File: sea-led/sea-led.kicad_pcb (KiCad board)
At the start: 2 copper layers, 0 parts

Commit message: Lots of footprint updates
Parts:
- added C1: 0.1uF, Capacitor_SMD:C_0805_2012Metric, F.Cu at (118.3, 56.6)
- added C10: 100uF, Capacitor_SMD:C_1206_3216Metric, F.Cu at (91.1, 74.0)
- added C11: 4.7uF, Capacitor_SMD:C_0805_2012Metric, F.Cu at (96.2, 73.8)
- added C12: 4.7uF, Capacitor_SMD:C_0805_2012Metric, F.Cu at (109.4, 59.6)
- added C13: 100uF, Capacitor_SMD:C_1206_3216Metric, F.Cu at (100.4, 64.9)
- added C14: 100uF, Capacitor_SMD:C_1206_3216Metric, F.Cu at (129.9, 37.2)
- added C15: 4700pF 2kV, Capacitor_SMD:C_1812_4532Metric, F.Cu at (116.9, 46.6)
- added C16: 0.01uF, Capacitor_SMD:C_0805_2012Metric, F.Cu at (116.8, 50.5)
- added C17: 330uF, Capacitor_Tantalum_SMD:CP_EIA-7343-30_AVX-N_Pad2.25x2.55mm_HandSolder, F.Cu at (93.6, 49.6)
- added C18: 0.01uF, Capacitor_SMD:C_0805_2012Metric, F.Cu at (105.4, 64.7)
- added C19: 10uF, Capacitor_SMD:C_0805_2012Metric, F.Cu at (135.0, 37.0)
- added C2: 22pF, Capacitor_SMD:C_0805_2012Metric, F.Cu at (121.3, 53.5)
- added C20: 1uF, Capacitor_SMD:C_0805_2012Metric, F.Cu at (109.4, 56.6)
- added C21: 0.1uF, Capacitor_SMD:C_0805_2012Metric, F.Cu at (131.5, 46.4)
- added C22: 0.1uF, Capacitor_SMD:C_0805_2012Metric, F.Cu at (125.7, 49.4)
- added C23: 0.1uF, Capacitor_SMD:C_0805_2012Metric, F.Cu at (133.8, 43.4)
- added C24: 0.1uF, Capacitor_SMD:C_0805_2012Metric, F.Cu at (91.1, 85.7)
- added C25: 0.1uF, Capacitor_SMD:C_0805_2012Metric, F.Cu at (114.3, 62.6)
- added C26: 2.2uF, Capacitor_SMD:C_0805_2012Metric, F.Cu at (105.1, 71.1)
- added C27: 0.1uF, Capacitor_SMD:C_0805_2012Metric, F.Cu at (98.3, 78.7)
- added C28: 0.1uF, Capacitor_SMD:C_0805_2012Metric, F.Cu at (125.7, 52.4)
- added C29: 0.1uF, Capacitor_SMD:C_0805_2012Metric, F.Cu at (129.3, 40.4)
- added C3: 0.1uF, Capacitor_SMD:C_0805_2012Metric, F.Cu at (100.6, 75.6)
- added C30: 10uF, Capacitor_SMD:C_0805_2012Metric, F.Cu at (121.3, 50.5)
- added C31: 1uF, Capacitor_SMD:C_0805_2012Metric, F.Cu at (113.8, 56.6)
- added C32: 0.1uF, Capacitor_SMD:C_0805_2012Metric, F.Cu at (103.6, 68.1)
- added C33: 0.1uF, Capacitor_SMD:C_0805_2012Metric, F.Cu at (89.2, 82.7)
- added C34: 0.1uF, Capacitor_SMD:C_0805_2012Metric, F.Cu at (93.8, 77.2)
- added C35: 0.1uF, Capacitor_SMD:C_0805_2012Metric, F.Cu at (129.3, 43.4)
- added C36: 0.1uF, Capacitor_SMD:C_0805_2012Metric, F.Cu at (100.6, 72.6)
- added C37: 0.1uF, Capacitor_SMD:C_0805_2012Metric, F.Cu at (93.8, 80.2)
- added C38: 0.1uF, Capacitor_SMD:C_0805_2012Metric, F.Cu at (113.8, 59.6)
- added C39: 0.1uF, Capacitor_SMD:C_0805_2012Metric, F.Cu at (116.8, 53.5)
- added C4: 1uF, Capacitor_SMD:C_0805_2012Metric, F.Cu at (127.1, 46.4)
- added C40: 0.1uF, Capacitor_SMD:C_0805_2012Metric, F.Cu at (109.9, 62.6)
- added C41: 0.1uF, Capacitor_SMD:C_0805_2012Metric, F.Cu at (86.7, 85.7)
- added C5: 22pF, Capacitor_SMD:C_0805_2012Metric, F.Cu at (133.8, 40.4)
- added C6: 5.5uF, Capacitor_SMD:C_0805_2012Metric, F.Cu at (65.5, 56.9)
- added C7: 2200uF, Custom:Panasonic-Electrolytic-K16, F.Cu at (52.7, 58.3)
- added C8: 100uF, Capacitor_SMD:C_1206_3216Metric, F.Cu at (111.8, 53.4)
- added C9: 4.7uF, Capacitor_SMD:C_0805_2012Metric, F.Cu at (122.6, 45.6)
- added D1: SMAJ30CA, Custom:SMAJ30CA, F.Cu at (111.2, 47.8)
- added D2: SMAJ30CA, Custom:SMAJ30CA, F.Cu at (65.5, 51.4)
- added D3: LED_ABGR, LED_SMD:LED_Cree-PLCC4_2x2mm_CW, F.Cu at (109.9, 66.1)
- added D4: PMEG045V100EPD, Custom:CFP15, F.Cu at (55.9, 81.4)
- added D5: BLUE - HSMN-C150, LED_SMD:LED_1206_3216Metric_Castellated, F.Cu at (68.0, 86.4)
- added D6: GREEN - HSMM-C150, LED_SMD:LED_1206_3216Metric_Castellated, F.Cu at (62.0, 86.4)
- added F1: Keystone - 3568, Custom:Keystone-3568, F.Cu at (50.9, 74.9)
- added F2: 2016L075/60MR, Custom:2016L075_60MR, F.Cu at (93.0, 69.3)
- added H1: MountingHole, MountingHole:MountingHole_3.5mm_Pad_Via, F.Cu at (104.7, 50.4)
- added H2: MountingHole, MountingHole:MountingHole_3.5mm_Pad_Via, F.Cu at (93.3, 61.9)
- added H3: MountingHole, MountingHole:MountingHole_3.5mm_Pad_Via, F.Cu at (84.0, 73.3)
- added H4: MountingHole, MountingHole:MountingHole_3.5mm_Pad_Via, F.Cu at (122.8, 39.8)
- added H5: MountingHole, MountingHole:MountingHole_3.5mm_Pad_Via, F.Cu at (102.9, 59.0)
- added H6: MountingHole, MountingHole:MountingHole_3.5mm_Pad_Via, F.Cu at (75.5, 77.1)
- added J1: TC2030-UART, Custom:TC2030-IDC-FP, F.Cu at (104.6, 40.8)
- added J2: TC-2050-Cortex-JTAG, Custom:TC2050-IDC-FP, F.Cu at (47.6, 84.2)
- added J3: Screw_Terminal_01x02, Custom:PhoenixContact-PTS-1_5-2POS-1703084, F.Cu at (65.5, 79.1)
- added J4: Screw_Terminal_01x05, Custom:PhoenixContact-PTS-1_5-5POS-1792892, F.Cu at (55.3, 41.8)
- added J5: Wurth_74980104400, Custom:Wurth_74980104400, F.Cu at (78.5, 47.2)
- added L1: 15uH SRP1265A-150M, Custom:SRP1265A-150M, F.Cu at (71.1, 65.8)
- added Q1: FDN5630, Package_TO_SOT_SMD:SOT-23, F.Cu at (99.1, 68.9)
- added R1: 10k, Resistor_SMD:R_0805_2012Metric, F.Cu at (113.9, 74.5)
- added R10: 145k, Resistor_SMD:R_0805_2012Metric, F.Cu at (109.5, 69.5)
- added R11: 30.1k, Resistor_SMD:R_0805_2012Metric, F.Cu at (105.0, 74.1)
- added R12: 10k, Resistor_SMD:R_0805_2012Metric, F.Cu at (118.3, 59.5)
- added R13: 10k, Resistor_SMD:R_0805_2012Metric, F.Cu at (130.2, 52.3)
- added R14: 10k, Resistor_SMD:R_0805_2012Metric, F.Cu at (109.5, 72.4)
- added R15: 2.4k, Resistor_SMD:R_0805_2012Metric, F.Cu at (122.7, 59.5)
- added R16: 4.87k, Resistor_SMD:R_0805_2012Metric, F.Cu at (136.0, 46.4)
- added R17: 6.6k, Resistor_SMD:R_0805_2012Metric, F.Cu at (127.1, 55.4)
- added R18: 49.9, Resistor_SMD:R_0805_2012Metric, F.Cu at (95.6, 87.5)
- added R19: 49.9, Resistor_SMD:R_0805_2012Metric, F.Cu at (114.3, 68.6)
- added R2: 10k, Resistor_SMD:R_0805_2012Metric, F.Cu at (131.5, 58.2)
- added R20: 49.9, Resistor_SMD:R_0805_2012Metric, F.Cu at (118.7, 65.6)
- added R21: 49.9, Resistor_SMD:R_0805_2012Metric, F.Cu at (102.7, 81.6)
- added R22: 1M, Resistor_SMD:R_0805_2012Metric, F.Cu at (98.3, 81.6)
- added R23: 330, Resistor_SMD:R_0805_2012Metric, F.Cu at (107.1, 77.0)
- added R24: 330, Resistor_SMD:R_0805_2012Metric, F.Cu at (127.1, 58.4)
- added R25: 330, Resistor_SMD:R_0805_2012Metric, F.Cu at (100.0, 84.6)
- added R26: 330, Resistor_SMD:R_0805_2012Metric, F.Cu at (123.2, 62.4)
- added R27: 10k, Resistor_SMD:R_0805_2012Metric, F.Cu at (134.6, 52.3)
- added R28: 3.16k, Resistor_SMD:R_0805_2012Metric, F.Cu at (113.9, 71.5)
- added R29: 51, Resistor_SMD:R_0805_2012Metric, F.Cu at (131.5, 55.3)
- added R3: 10k, Resistor_SMD:R_0805_2012Metric, F.Cu at (118.7, 68.6)
- added R30: 10k, Resistor_SMD:R_0805_2012Metric, F.Cu at (100.0, 87.5)
- added R31: 100, Resistor_SMD:R_0805_2012Metric, F.Cu at (107.1, 80.0)
- added R32: 10k, Resistor_SMD:R_0805_2012Metric, F.Cu at (134.6, 49.4)
- added R33: 100, Resistor_SMD:R_0805_2012Metric, F.Cu at (123.1, 65.4)
- added R4: 120, Resistor_SMD:R_0805_2012Metric, F.Cu at (122.7, 56.5)
- added R5: 100, Resistor_SMD:R_0805_2012Metric, F.Cu at (118.8, 62.5)
- added R6: 100, Resistor_SMD:R_0805_2012Metric, F.Cu at (102.7, 78.6)
- added R7: 100, Resistor_SMD:R_0805_2012Metric, F.Cu at (130.2, 49.4)
- added R8: 100, Resistor_SMD:R_0805_2012Metric, F.Cu at (95.6, 84.6)
- added R9: 706k, Resistor_SMD:R_0805_2012Metric, F.Cu at (114.3, 65.6)
- added SW1: SW_Push, Custom:PTS636, F.Cu at (83.9, 61.3)
- added SW2: SW_Push, Custom:PTS636, F.Cu at (93.5, 55.1)
- added SW3: SW_Push, Custom:PTS636, F.Cu at (83.9, 66.4)
- added TP1: TestPoint, TestPoint:TestPoint_Pad_D1.5mm, F.Cu at (117.9, 71.8)
- added TP2: TestPoint, TestPoint:TestPoint_Pad_D1.5mm, F.Cu at (104.0, 84.8)
- added TP3: TestPoint, TestPoint:TestPoint_Pad_D1.5mm, F.Cu at (127.1, 61.6)
- added TP4: TestPoint, TestPoint:TestPoint_Pad_D1.5mm, F.Cu at (111.1, 77.7)
- added TP5: TestPoint, TestPoint:TestPoint_Pad_D1.5mm, F.Cu at (135.5, 55.6)
- added TP6: TestPoint, TestPoint:TestPoint_Pad_D1.5mm, F.Cu at (122.7, 68.7)
- added U1: TM4C129ENCZADI3R, TM4C:TM4C129ENCZADI3R, F.Cu at (94.8, 41.1)
- added U2: THVD2450, Custom:VSON-8, F.Cu at (89.3, 79.4)
- added U3: TPS2660, Custom:VQFN-24, F.Cu at (83.3, 80.6)
- added U4: TPS5450, Custom:PowerPAD-SOIC-8, F.Cu at (75.3, 84.5)
- added U5: TL1963A-33DCYR, Package_TO_SOT_SMD:SOT-223-3_TabPin2, F.Cu at (113.6, 39.7)
- added Y1: LFXTAL071758Cutt, Custom:LFXTAL071758CUTT, F.Cu at (82.0, 85.8)

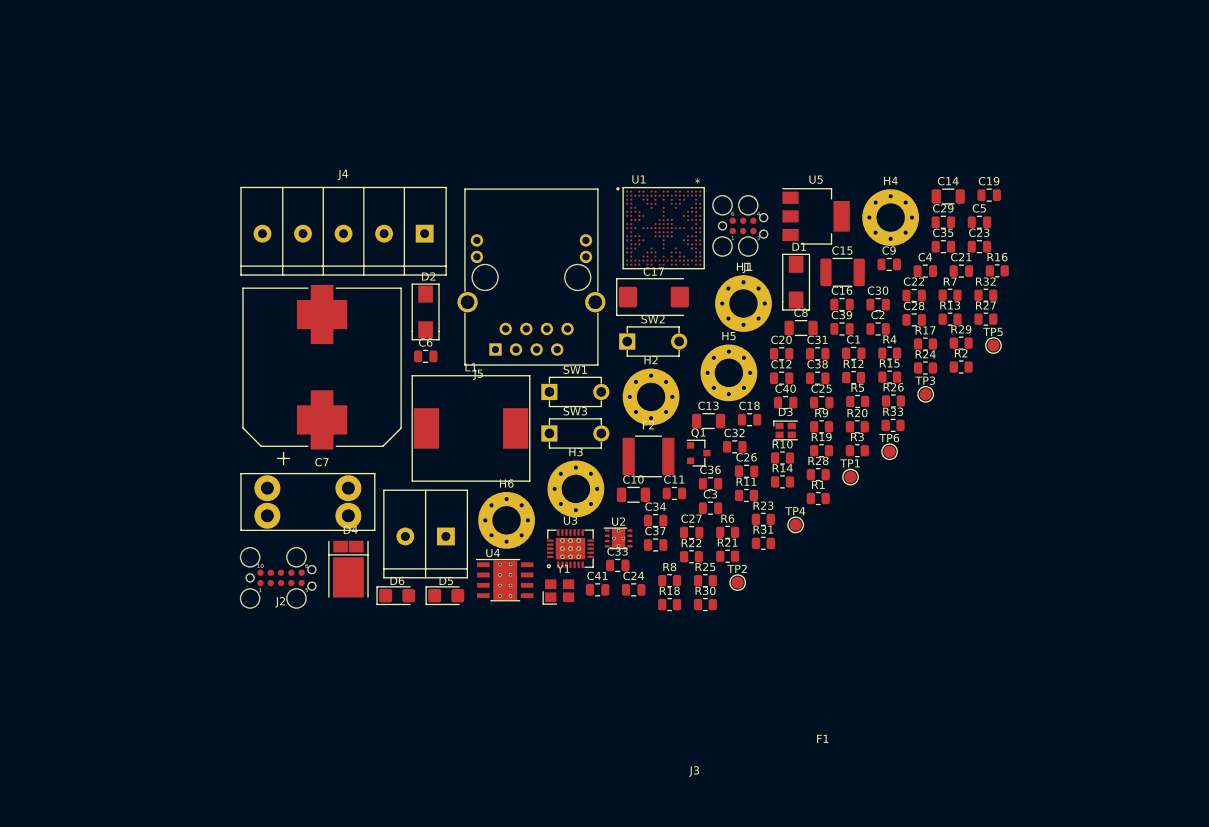
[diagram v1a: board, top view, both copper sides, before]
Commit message: Sea LED Routing Complete
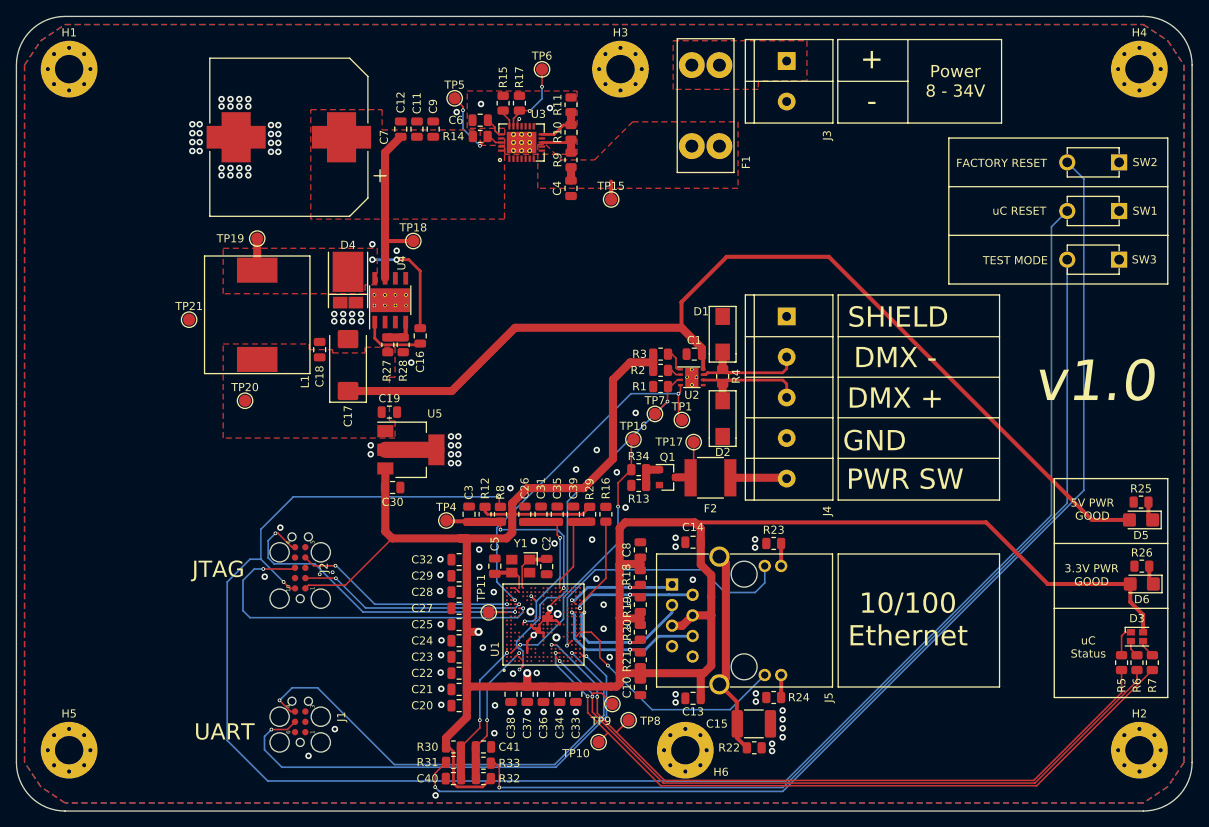
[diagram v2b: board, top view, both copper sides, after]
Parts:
- removed TP2, TP3: TestPoint, TestPoint:TestPoint_Pad_D1.5mm
- added G***: LOGO, TM4C:SEA_LED, F.Cu at (26.0, 62.0)
- added R34: 100, Resistor_SMD:R_0805_2012Metric, F.Cu at (91.8, 70.9)
- added TP10: TestPoint, TestPoint:TestPoint_Pad_D1.5mm, F.Cu at (86.8, 104.5)
- added TP11: TestPoint, TestPoint:TestPoint_Pad_D1.5mm, F.Cu at (73.2, 88.5)
- added TP15: TestPoint, TestPoint:TestPoint_Pad_D1.5mm, F.Cu at (88.3, 37.6)
- added TP16: TestPoint, TestPoint:TestPoint_Pad_D1.5mm, F.Cu at (91.1, 67.2)
- added TP17: TestPoint, TestPoint:TestPoint_Pad_D1.5mm, F.Cu at (98.5, 67.5)
- added TP18: TestPoint, TestPoint:TestPoint_Pad_D1.5mm, F.Cu at (64.0, 42.7)
- added TP19: TestPoint, TestPoint:TestPoint_Pad_D1.5mm, F.Cu at (44.7, 42.4)
- added TP20: TestPoint, TestPoint:TestPoint_Pad_D1.5mm, F.Cu at (43.2, 62.4)
- added TP21: TestPoint, TestPoint:TestPoint_Pad_D1.5mm, F.Cu at (36.3, 52.4)
- added TP7: TestPoint, TestPoint:TestPoint_Pad_D1.5mm, F.Cu at (93.8, 64.0)
- added TP8: TestPoint, TestPoint:TestPoint_Pad_D1.5mm, F.Cu at (90.5, 101.8)
- added TP9: TestPoint, TestPoint:TestPoint_Pad_D1.5mm, F.Cu at (88.5, 99.8)
- C10, C13, C14, C8: value 100uF -> 0.1uF; footprint Capacitor_SMD:C_1206_3216Metric -> Capacitor_SMD:C_0805_2012Metric
- C2, C5: value 22pF -> 8pF
- moved H5 93.7 mm to (21.5, 105.5)
- moved D6 91.8 mm to (153.8, 85.0), turned to 180 degrees
- moved H1 88.1 mm to (21.5, 21.5)
- moved D5 86.2 mm to (153.7, 77.1), turned to 180 degrees
- moved R32 86.0 mm to (72.6, 109.0), turned to 180 degrees
- moved J1 82.0 mm to (50.0, 102.0), turned to 90 degrees
- moved C23 81.7 mm to (69.6, 94.0), turned to 180 degrees
- moved C21 80.6 mm to (69.6, 98.0), turned to 180 degrees
- moved C19 78.7 mm to (61.0, 63.8)
- moved H2 74.3 mm to (153.5, 105.5)
- moved C29 73.9 mm to (69.6, 84.0), turned to 180 degrees
- moved R27 73.8 mm to (60.8, 55.5), turned to 90 degrees
- moved C5 73.3 mm to (74.0, 82.8), turned to 90 degrees
- moved TP5 73.1 mm to (69.0, 25.1)
- moved C22 72.9 mm to (69.6, 96.0), turned to 180 degrees
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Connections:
- net Net-(J5-Pad1) renamed /ETH_TX_P
- net Net-(J5-Pad2) renamed /ETH_TX_N
- net Net-(J5-Pad3) renamed /ETH_RX_P
- net Net-(J5-Pad6) renamed /ETH_RX_N
- C3 pad 1: /JTAG_RESET -> Net-(C3-Pad1)
- D3 pad 1: +3V3 -> Net-(D3-Pad1)
- D3 pad 2: Net-(D3-Pad2) -> +3V3
- J2 pad 1: (no net) -> +3V3
- Q1 pad 1: /PWR_SW_CTL -> Net-(Q1-Pad1)
- R1 pad 1: +3V3 -> /DMX_TX_EN
- R1 pad 2: Net-(R1-Pad2) -> GND
- R12 pad 2: /JTAG_RESET -> Net-(C3-Pad1)
- R13 pad 1: /PWR_SW_CTL -> Net-(Q1-Pad1)
- R5 pad 1: /IND_G -> /IND_R
- R5 pad 2: Net-(D3-Pad3) -> Net-(D3-Pad1)
- R6 pad 1: /IND_R -> /IND_G
- R7 pad 2: Net-(D3-Pad2) -> Net-(D3-Pad3)
- R8 pad 1: /JTAG_RESET -> Net-(C3-Pad1)
- R8 pad 2: Net-(R8-Pad2) -> /JTAG_RESET
- SW1 pad 2: Net-(R8-Pad2) -> /JTAG_RESET
- SW2 pad 1: Net-(R31-Pad2) -> GND
- SW2 pad 2: GND -> Net-(R31-Pad2)
- SW3 pad 1: Net-(R33-Pad2) -> GND
- SW3 pad 2: GND -> Net-(R33-Pad2)
- TP4 pad 1: /JTAG_RESET -> Net-(C3-Pad1)
- U1 pad A13: (no net) -> /DIVSCLK
- U1 pad B2: /PWR_SW_CTL -> (no net)
- U1 pad B3: (no net) -> /PWR_SW_CTL
- U1 pad D19: (no net) -> Net-(C5-Pad1)
- U1 pad D2: (no net) -> /DMX_TX_EN
- U1 pad E19: GND -> Net-(C2-Pad1)
- U1 pad P18: /JTAG_RESET -> Net-(C3-Pad1)
- U1 pad T18: Net-(C2-Pad1) -> GND
- U1 pad T19: Net-(C5-Pad1) -> (no net)
- U2 pad 3: Net-(R1-Pad2) -> /DMX_TX_EN
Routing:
- net +3V3: track 0.00 -> 322.6 mm, vias 0 -> 4
- net /JTAG_RESET: track 0.00 -> 222.2 mm, vias 0 -> 2
- net Net-(R31-Pad2): track 0.00 -> 140.5 mm, vias 0 -> 1
- net +5V: track 0.00 -> 124.8 mm
- net Net-(R33-Pad2): track 0.00 -> 118.4 mm, vias 0 -> 1
- net /IND_B: track 0.00 -> 90.4 mm, vias 0 -> 2
- net /IND_G: track 0.00 -> 89.4 mm, vias 0 -> 2
- net /IND_R: track 0.00 -> 89.1 mm, vias 0 -> 2
- net /UART_TX: track 0.00 -> 61.3 mm, vias 0 -> 2
- net /UART_RX: track 0.00 -> 59.4 mm, vias 0 -> 2
- net /DMX_TX_EN: track 0.00 -> 50.2 mm, vias 0 -> 2
- net /JTAG_TDI: track 0.00 -> 46.9 mm, vias 0 -> 2
- net /DMX_TX: track 0.00 -> 44.2 mm, vias 0 -> 2
- net /JTAG_TDO: track 0.00 -> 40.2 mm, vias 0 -> 2
- net /ETH_LED1: track 0.00 -> 36.3 mm, vias 0 -> 1
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- added copper zone on F.Cu, net +12V
- added copper zone on F.Cu, net +5V
- added copper zone on F.Cu, net +BATT
- added copper zone on B.Cu, net GND
- added copper zone on F.Cu, net GND
- added copper zone on In1.Cu, net GND
- added copper zone on In2.Cu, net GND
- added copper zone on F.Cu, net Net-(C16-Pad1)
- added copper zone on F.Cu, net Net-(C4-Pad1)
- added copper zone on F.Cu, net Net-(C6-Pad2)
- added copper zone on In2.Cu, net Net-(C6-Pad2)
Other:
- board outline added: 145 x 98 mm
- copper layers 2 -> 4
- net class ETH added: clearance 0.127, trace_width 0.127, via_dia 0.8, via_drill 0.4
- board text added: "+"
- board text added: "-"
- board text added: "10/100 Ethernet"
- board text added: "3.3V PWR GOOD"
- board text added: "5V PWR GOOD"
- board text added: "DMX +"
- board text added: "DMX -"
- board text added: "FACTORY RESET"
- board text added: "GND"
- board text added: "JTAG"
- board text added: "PWR SW"
- board text added: "Power 8 - 34V"
- board text added: "SHIELD"
- board text added: "TEST MODE"
- board text added: "UART"
- board text added: "uC RESET"
- board text added: "uC Status"
- board text added: "v1.0"
